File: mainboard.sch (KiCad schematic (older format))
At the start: 71 parts, among them J1 Conn_01x06, J2 USB_B_Micro, J3 xf2m-2415-1a, J4 XF2M-1015-1A, J5 Conn_01x02, J6 U.FL-R-SMT-1, Q1 RADFET, SW1 KMR231NG LFS, U1 BMX160, U10 TPS82740BSIPR, U2 MAX708RESA-T, U3 ATSAMD51J20A-M, U4 DRV8830DRC, U5 MR25H40, U6 DRV8830DRC, U7 ADS124S06IRHBR, U8 DRV8830DRC, U9 RFM98PW-symbols

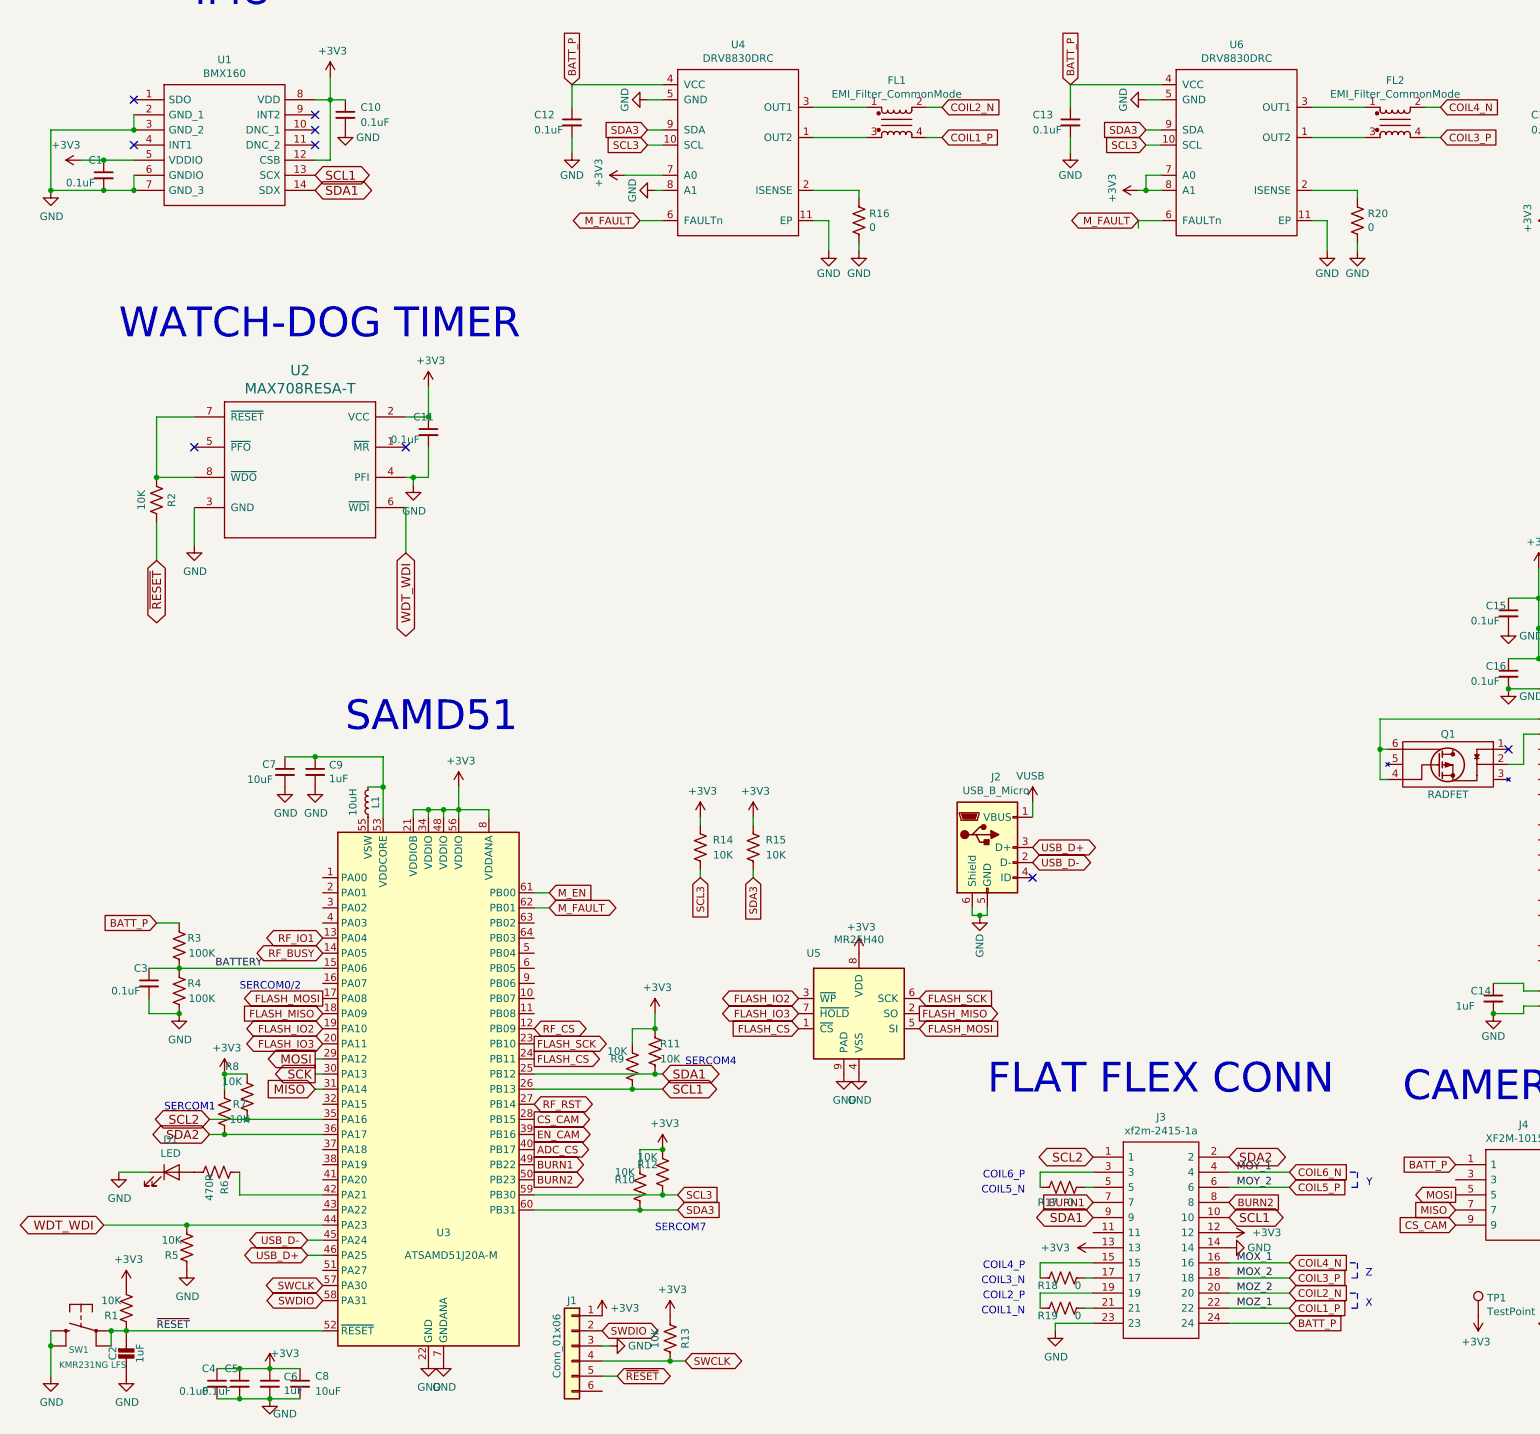
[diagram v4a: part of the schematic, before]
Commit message: layout minus dosimeter
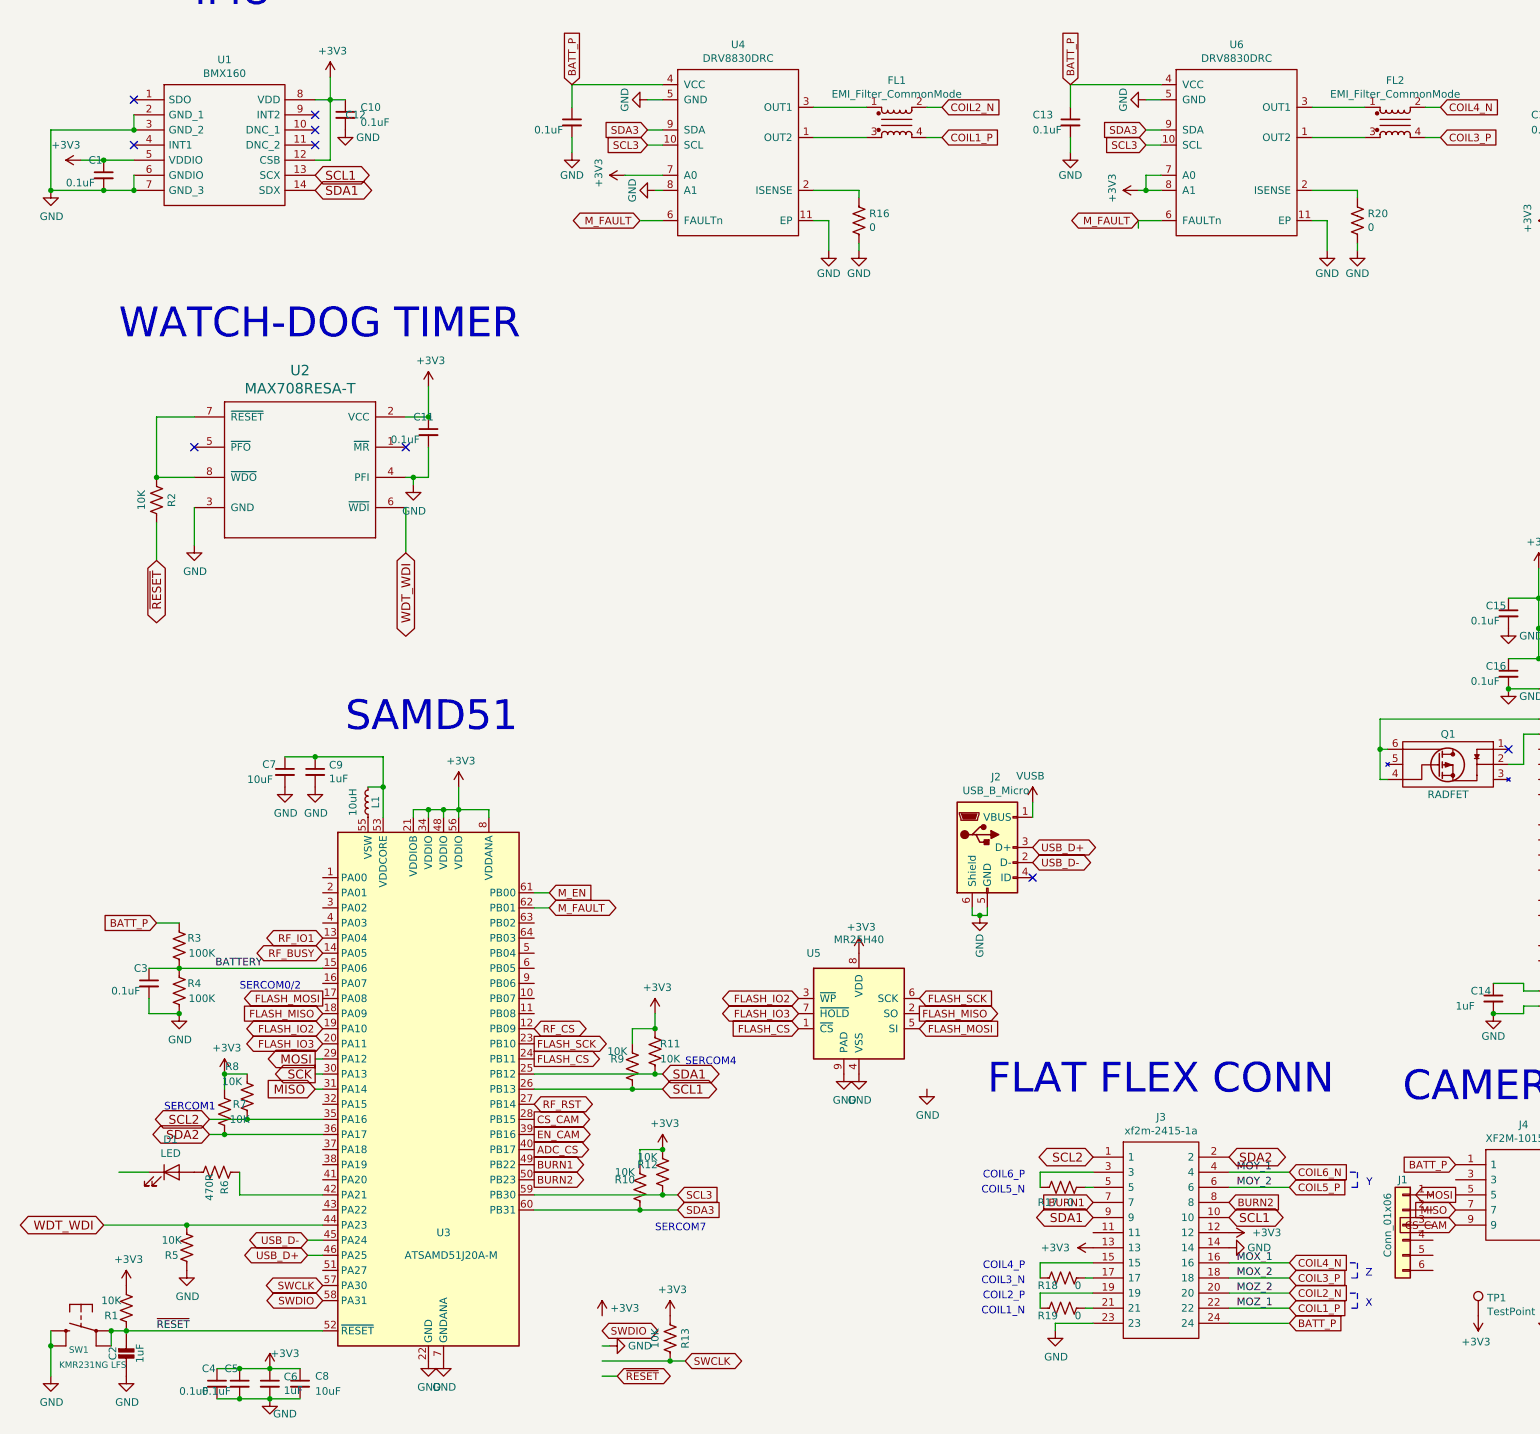
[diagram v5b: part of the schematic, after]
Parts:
- removed R14, R15: 10K, Resistor_SMD:R_0402_1005Metric, symbol mainboard-rescue:R_US-Device
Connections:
- net +3V3: no longer J1.1 (Pin_1)
- net GND: no longer D1.1 (K), J1.3 (Pin_3)
- net SWCLK: no longer J1.4 (Pin_4)
- net SWDIO: no longer J1.2 (Pin_2)
- net ~RESET: no longer J1.5 (Pin_5)
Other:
- moved on the sheet: J1
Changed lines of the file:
@@
 L Connector_Generic:Conn_01x06 J1
 U 1 1 5DB917BE
-P 4100 10000
-F 0 "J1" H 4100 10300 50  0000 C CNN
-F 1 "Conn_01x06" V 4200 10000 50  0000 C CNN
-F 2 "Connector_PinHeader_1.27mm:PinHeader_2x03_P1.27mm_Vertical_SMD" H 4100 10000 50  0001 C CNN
-F 3 "~" H 4100 10000 50  0001 C CNN
-	1    4100 10000
+P 9600 9200
+F 0 "J1" H 9600 9500 50  0000 C CNN
+F 1 "Conn_01x06" V 9700 9200 50  0000 C CNN
+F 2 "Connector_PinHeader_1.27mm:PinHeader_2x03_P1.27mm_Vertical_SMD" H 9600 9200 50  0001 C CNN
+F 3 "~" H 9600 9200 50  0001 C CNN
+	1    9600 9200
 	-1   0    0    -1
 $EndComp
@@
 Text Notes 9600 8400 0    197  ~ 0
 CAMERA CONN
-$Comp
-L mainboard-rescue:ADS124S06IRHBR-symbols U7
-U 1 1 5E004790
-P 11500 6350
-F 0 "U7" H 11500 6350 50  0001 C CNN
-F 1 "ADS124S06IRHBR" H 11500 6350 50  0001 C CNN
-F 2 "custom-footprints:ADS124208_withpad" H 11500 6350 50  0001 C CNN
-F 3 "" H 11500 6350 50  0001 C CNN
-	1    11500 6350
-	1    0    0    -1
-$EndComp
 Wire Wire Line
 	10500 5450 10500 5250
@@
 Text GLabel 4800 9100 2    50   Input ~ 0
 SDA3
-$Comp
-L mainboard-rescue:R_US-Device R15
-U 1 1 5E57D0AA
-P 5300 6700
-F 0 "R15" H 5150 6650 50  0000 C CNN
-F 1 "10K" H 5150 6750 50  0000 C CNN
-F 2 "Resistor_SMD:R_0402_1005Metric" V 5340 6690 50  0001 C CNN
-F 3 "~" H 5300 6700 50  0001 C CNN
-	1    5300 6700
-	-1   0    0    1
-$EndComp
-$Comp
-L mainboard-rescue:R_US-Device R14
-U 1 1 5E57D451
-P 4950 6700
-F 0 "R14" H 4800 6650 50  0000 C CNN
-F 1 "10K" H 4800 6750 50  0000 C CNN
-F 2 "Resistor_SMD:R_0402_1005Metric" V 4990 6690 50  0001 C CNN
-F 3 "~" H 4950 6700 50  0001 C CNN
-	1    4950 6700
-	-1   0    0    1
-$EndComp
-Text GLabel 4950 6900 3    50   Input ~ 0
-SCL3
-Text GLabel 5300 6900 3    50   Input ~ 0
-SDA3
-$Comp
-L power:+3V3 #PWR031
-U 1 1 5E589809
-P 4950 6500
-F 0 "#PWR031" H 4950 6350 50  0001 C CNN
-F 1 "+3V3" H 4965 6673 50  0000 C CNN
-F 2 "" H 4950 6500 50  0001 C CNN
-F 3 "" H 4950 6500 50  0001 C CNN
-	1    4950 6500
-	1    0    0    -1
-$EndComp
-$Comp
-L power:+3V3 #PWR032
-U 1 1 5E589890
-P 5300 6500
-F 0 "#PWR032" H 5300 6350 50  0001 C CNN
-F 1 "+3V3" H 5315 6673 50  0000 C CNN
-F 2 "" H 5300 6500 50  0001 C CNN
-F 3 "" H 5300 6500 50  0001 C CNN
-	1    5300 6500
-	1    0    0    -1
-$EndComp
-Wire Wire Line
-	4950 6500 4950 6550
-Wire Wire Line
-	5300 6500 5300 6550
-Wire Wire Line
-	5300 6850 5300 6900
-Wire Wire Line
-	4950 6850 4950 6900
 Text GLabel 11200 1950 0    50   Input ~ 0
 SDA3
@@
 U 1 1 5E74915D
 P 4100 1900
-F 0 "C12" H 3850 1950 50  0000 L CNN
+F 0 "C12" H 2600 1950 50  0000 L CNN
 F 1 "0.1uF" H 3850 1850 50  0000 L CNN
 F 2 "Capacitor_SMD:C_0402_1005Metric" H 4100 1900 50  0001 C CNN
@@
 Text GLabel 13150 1800 2    50   Input ~ 0
 COIL6_N
-$Comp
-L MCU_Microchip_SAMD:ATSAMD51J20A-M U3
-U 1 1 5F37375A
-P 3150 8300
-F 0 "U3" H 3250 7350 50  0000 C CNN
-F 1 "ATSAMD51J20A-M" H 3300 7200 50  0000 C CNN
-F 2 "Package_DFN_QFN:QFN-64-1EP_9x9mm_P0.5mm_EP4.7x4.7mm" H 3150 8300 50  0001 C CIN
-F 3 "http://ww1.microchip.com/downloads/en/DeviceDoc/60001507E.pdf" H 3150 8300 50  0001 C CNN
-	1    3150 8300
-	1    0    0    -1
-$EndComp
 $Comp
 L power:+3V3 #PWR021
@@
 L power:GND #PWR04
 U 1 1 5F73E007
-P 1100 8850
-F 0 "#PWR04" H 1100 8600 50  0001 C CNN
-F 1 "GND" H 1105 8677 50  0000 C CNN
-F 2 "" H 1100 8850 50  0001 C CNN
-F 3 "" H 1100 8850 50  0001 C CNN
-	1    1100 8850
+P 6450 8300
+F 0 "#PWR04" H 6450 8050 50  0001 C CNN
+F 1 "GND" H 6455 8127 50  0000 C CNN
+F 2 "" H 6450 8300 50  0001 C CNN
+F 3 "" H 6450 8300 50  0001 C CNN
+	1    6450 8300
 	1    0    0    -1
 $EndComp
@@
 	1    0    0    -1
 $EndComp
+$Comp
+L MCU_Microchip_SAMD:ATSAMD51J20A-M U3
+U 1 1 5F37375A
+P 3150 8300
+F 0 "U3" H 3250 7350 50  0000 C CNN
+F 1 "ATSAMD51J20A-M" H 3300 7200 50  0000 C CNN
+F 2 "Package_DFN_QFN:QFN-64-1EP_9x9mm_P0.5mm_EP4.7x4.7mm" H 3150 8300 50  0001 C CIN
+F 3 "http://ww1.microchip.com/downloads/en/DeviceDoc/60001507E.pdf" H 3150 8300 50  0001 C CNN
+	1    3150 8300
+	1    0    0    -1
+$EndComp
+$Comp
+L mainboard-rescue:ADS124S06IRHBR-symbols U7
+U 1 1 5E004790
+P 11500 6350
+F 0 "U7" H 11500 6350 50  0001 C CNN
+F 1 "ADS124S06IRHBR" H 11500 6350 50  0001 C CNN
+F 2 "custom-footprints:ADS124208_withpad" H 11500 6350 50  0001 C CNN
+F 3 "" H 11500 6350 50  0001 C CNN
+	1    11500 6350
+	1    0    0    -1
+$EndComp

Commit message: RGB LED
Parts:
- removed D1: LED, LED_SMD:LED_0805_2012Metric, symbol Device:LED
- removed R6: 470R, Resistor_SMD:R_0402_1005Metric, symbol mainboard-rescue:R_US-Device
- added D1: WS2812B, LED_SMD:LED_WS2812B_PLCC4_5.0x5.0mm_P3.2mm, symbol LED:WS2812B
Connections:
- net +3V3: now also J1.1 (Pin_1), D1.1 (VDD)
- net GND: now also J1.3 (Pin_3), D1.3 (VSS)
- net SWCLK: now also J1.4 (Pin_4)
- net SWDIO: now also J1.2 (Pin_2)
- net ~RESET: now also J1.5 (Pin_5)
- net at U3.42 (PA21): now also D1.4 (DIN)
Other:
- moved on the sheet: J1
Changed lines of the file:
@@
 L Connector_Generic:Conn_01x06 J1
 U 1 1 5DB917BE
-P 9600 9200
-F 0 "J1" H 9600 9500 50  0000 C CNN
-F 1 "Conn_01x06" V 9700 9200 50  0000 C CNN
-F 2 "Connector_PinHeader_1.27mm:PinHeader_2x03_P1.27mm_Vertical_SMD" H 9600 9200 50  0001 C CNN
-F 3 "~" H 9600 9200 50  0001 C CNN
-	1    9600 9200
+P 4100 10000
+F 0 "J1" H 4100 10300 50  0000 C CNN
+F 1 "Conn_01x06" V 4200 10000 50  0000 C CNN
+F 2 "Connector_PinHeader_1.27mm:PinHeader_2x03_P1.27mm_Vertical_SMD" H 4100 10000 50  0001 C CNN
+F 3 "~" H 4100 10000 50  0001 C CNN
+	1    4100 10000
 	-1   0    0    -1
 $EndComp
@@
 $EndComp
 $Comp
-L Device:LED D1
-U 1 1 5F632E2F
-P 1450 8850
-F 0 "D1" H 1443 9066 50  0000 C CNN
-F 1 "LED" H 1443 8975 50  0000 C CNN
-F 2 "LED_SMD:LED_0805_2012Metric" H 1450 8850 50  0001 C CNN
-F 3 "~" H 1450 8850 50  0001 C CNN
-	1    1450 8850
-	1    0    0    -1
-$EndComp
-$Comp
-L mainboard-rescue:R_US-Device R6
-U 1 1 5F68B037
-P 1750 8850
-F 0 "R6" H 1850 8900 50  0000 C CNN
-F 1 "470R" H 1850 8800 50  0000 C CNN
-F 2 "Resistor_SMD:R_0402_1005Metric" V 1790 8840 50  0001 C CNN
-F 3 "~" H 1750 8850 50  0001 C CNN
-	1    1750 8850
-	0    1    1    0
-$EndComp
-Wire Wire Line
-	2450 9000 1900 9000
-Wire Wire Line
-	1900 9000 1900 8850
-$Comp
 L power:GND #PWR04
 U 1 1 5F73E007
@@
 $EndComp
 Wire Wire Line
-	1300 8850 1100 8850
-Wire Wire Line
 	10700 2000 10700 2100
 $Comp
@@
 	1    0    0    -1
 $EndComp
+$Comp
+L LED:WS2812B D1
+U 1 1 5F467C19
+P 900 8650
+F 0 "D1" H 556 8696 50  0000 R CNN
+F 1 "WS2812B" H 556 8605 50  0000 R CNN
+F 2 "LED_SMD:LED_WS2812B_PLCC4_5.0x5.0mm_P3.2mm" H 950 8350 50  0001 L TNN
+F 3 "https://cdn-shop.adafruit.com/datasheets/WS2812B.pdf" H 1000 8275 50  0001 L TNN
+	1    900  8650
+	-1   0    0    -1
+$EndComp
+Wire Wire Line
+	1200 9000 2450 9000
+$Comp
+L power:GND #PWR0101
+U 1 1 5F53A22F
+P 900 8950
+F 0 "#PWR0101" H 900 8700 50  0001 C CNN
+F 1 "GND" H 905 8777 50  0000 C CNN
+F 2 "" H 900 8950 50  0001 C CNN
+F 3 "" H 900 8950 50  0001 C CNN
+	1    900  8950
+	1    0    0    -1
+$EndComp
+$Comp
+L power:+3V3 #PWR0102
+U 1 1 5F53A694
+P 900 8350
+F 0 "#PWR0102" H 900 8200 50  0001 C CNN
+F 1 "+3V3" H 915 8523 50  0000 C CNN
+F 2 "" H 900 8350 50  0001 C CNN
+F 3 "" H 900 8350 50  0001 C CNN
+	1    900  8350
+	1    0    0    -1
+$EndComp
+Wire Wire Line
+	1200 9000 1200 8650
 $EndSCHEMATC
